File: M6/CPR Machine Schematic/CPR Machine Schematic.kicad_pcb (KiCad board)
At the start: 2 copper layers, 79.8 x 63 mm, 78 parts, among them J1 Battery 22.2V IN, J10 Stop Button Port, J11 Go Button Port, J12 I2C Port, J13 Raspberry_Pi_2_3, J15 Conn_02x20_Odd_Even, J2 5V Spare Headers, J3 Power Switch, J4 3V3 Spare Headers, J5 12 Spare headers, J6 Battery Spare headers, J7 GND Spare Headers, J8 Force Sensor, J9 Laser Port, Q2 SSM3J332R, Q3 T2N7002BK,LM, Q4 DMMT5401 PNP, Q5 DMMT5401 PNP, Q6 T2N7002BK,LM, Q7 T2N7002BK,LM, Q8 DMG2305UX-EV, U2 MAX42403AFLB+, U3 MCP6004, U4 12V Buck, U5 MCP3021A0T-E_OT, U6 3.3V Buck

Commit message: XT30 Connectors to battery instead of screw term
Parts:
- J1, J3: footprint TerminalBlock:TerminalBlock_MaiXu_MX126-5.0-02P_1x02_P5.00mm -> Connector_AMASS:AMASS_XT30PW-M_1x02_P2.50mm_Horizontal
- moved TP4 9.79 mm to (125.0, 75.5)
- moved TP1 6.11 mm to (130.8, 75.5)
- moved TP3 5.92 mm to (118.1, 82.5)
- moved U6 5.75 mm to (126.8, 88.0)
- moved TP2 5.58 mm to (118.1, 88.9)
- moved J3 4.62 mm to (118.5, 97.0), turned to 90 degrees
- moved J1 1.86 mm to (118.5, 111.5), turned to 90 degrees
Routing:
- net +12V: track 83.3 -> 86.3 mm, vias 2 -> 3
- net +3.3V: track 189.4 -> 186.4 mm
- net /Power/From Switch: track 12.5 -> 15.5 mm
- net +22.2V: track 133.1 -> 130.6 mm
- net /Power/Battery +: track 7.47 -> 9.03 mm
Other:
- board size 79.8 x 63 mm -> 89.9 x 63 mm

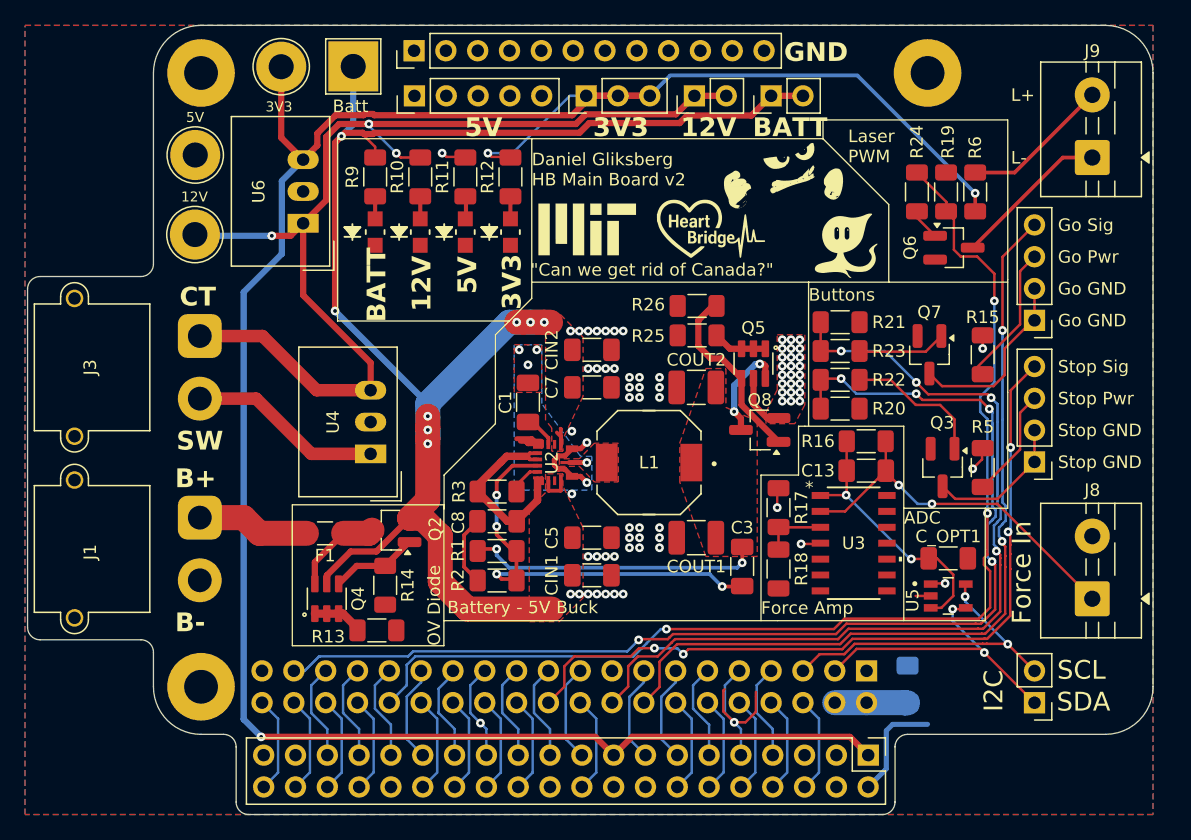
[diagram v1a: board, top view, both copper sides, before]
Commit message: Updated ADC Logic Level, Redone Layout, Geographic Reannotation
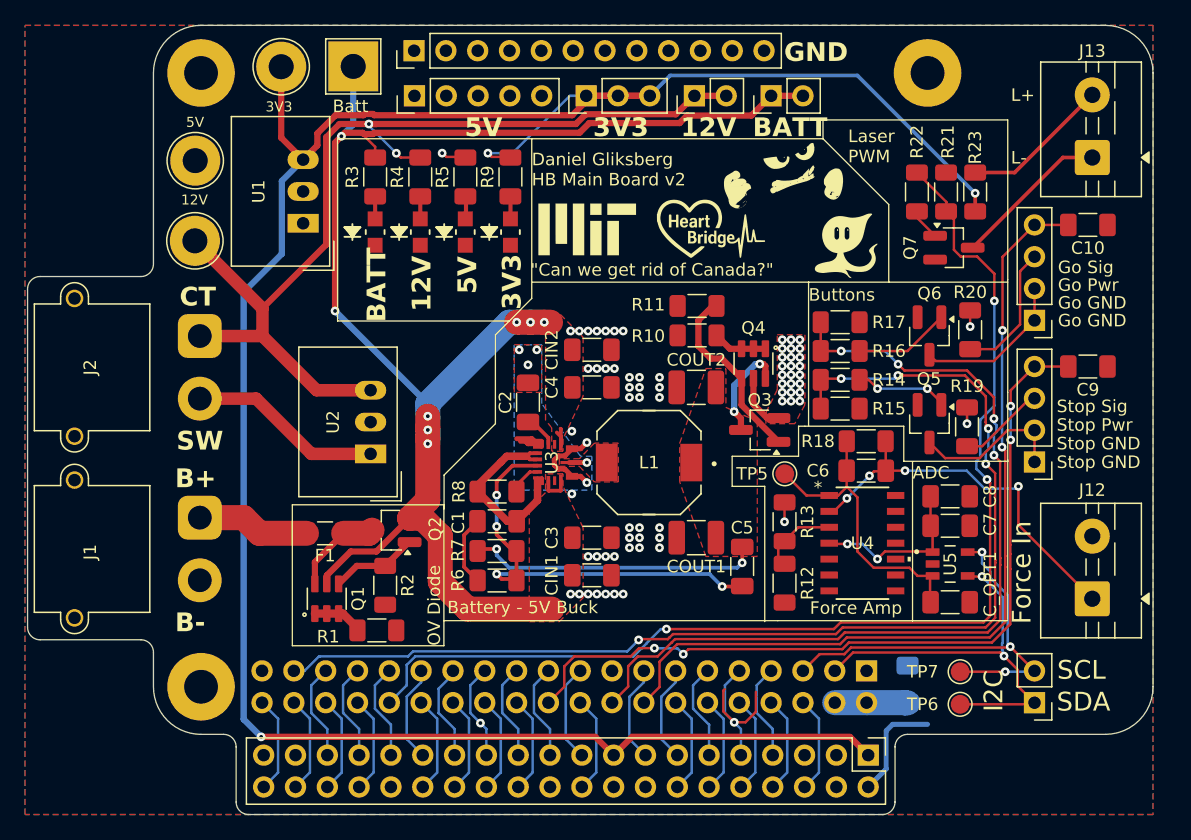
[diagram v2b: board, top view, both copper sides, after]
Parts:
- added C10: 100 nF, Capacitor_SMD:C_1206_3216Metric_Pad1.33x1.80mm_HandSolder, F.Cu at (189.4, 88.1)
- added C7: 0.1 uF, Capacitor_SMD:C_1206_3216Metric_Pad1.33x1.80mm_HandSolder, F.Cu at (178.4, 112.2)
- added C8: 10 uF, Capacitor_SMD:C_1206_3216Metric_Pad1.33x1.80mm_HandSolder, F.Cu at (178.4, 109.8)
- added C9: 100 nF, Capacitor_SMD:C_1206_3216Metric_Pad1.33x1.80mm_HandSolder, F.Cu at (189.4, 99.4)
- added TP5: Amp Out, TestPoint:TestPoint_Pad_D1.5mm, F.Cu at (165.2, 108.0)
- added TP6: SDA, TestPoint:TestPoint_Pad_D1.5mm, F.Cu at (179.2, 126.4)
- added TP7: SCL, TestPoint:TestPoint_Pad_D1.5mm, F.Cu at (179.2, 123.8)
- moved Q5 3.65 mm to (176.8, 104.0)
- moved C_OPT1 3.50 mm to (178.4, 118.2)
- moved R19 3.48 mm to (179.8, 104.2)
- moved U5 2.55 mm to (178.4, 115.2)
- moved R20 2.24 mm to (180.0, 96.5)
- moved Q6 1.50 mm to (176.8, 97.0)
- moved R12 1.23 mm to (165.2, 116.7)
- moved R13 1.23 mm to (165.2, 111.8)
- moved U4 0.70 mm to (171.4, 113.5)
- moved TP1 0.50 mm to (118.1, 89.4)
- moved TP2 0.45 mm to (118.1, 83.0)
- renumbered C8 to C1, C1 to C2, C5 to C3, C7 to C4, C3 to C5, C13 to C6, H4 to H1, H3 to H2, H1 to H3, J8 to J12, J9 to J13, J13 to J14, J3 to J2, J2 to J3, J7 to J4, J4 to J5, J5 to J6, J6 to J7, J15 to J8, J12 to J9, Q4 to Q1, Q8 to Q3, Q5 to Q4, Q3 to Q5, Q7 to Q6, Q6 to Q7, R13 to R1, R25 to R10, R26 to R11, R18 to R12, R17 to R13, R22 to R14, R20 to R15, R23 to R16, R21 to R17, R16 to R18, R5 to R19, R14 to R2, R15 to R20, R19 to R21, R24 to R22, R6 to R23, R9 to R3, R10 to R4, R11 to R5, R2 to R6, R1 to R7, R3 to R8, R12 to R9, TP2 to TP1, TP3 to TP2, TP4 to TP3, TP1 to TP4, U6 to U1, U4 to U2, U2 to U3, U3 to U4
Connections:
- U1 pad 1: +12V -> +5V
- U4 pad 4: +5V -> +3V3
- U5 pad 1: +5V -> +3V3
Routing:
- net +3V3: track 0.00 -> 13.6 mm, vias 0 -> 2
- net /Raspi/I2C_SCL: track 26.5 -> 35.7 mm, vias 2 -> 3
- net /Raspi/I2C_SDA: track 24.1 -> 33.2 mm
- net +12V: track 86.3 -> 80.2 mm, vias 3 -> 2
- net +5V: track 22.7 -> 19.3 mm, vias 30 -> 28
- net Net-(Q3-G): track 11.2 -> 8.18 mm, vias 0 -> 2
- net /HMI_Raspi/Stop Button: track 62.0 -> 64.9 mm
- net Net-(U5-AIN): track 21.5 -> 24.3 mm, vias 2 -> 0
- net /HMI_Raspi/Go Button: track 65.6 -> 68.3 mm
- net /HMI_Raspi/Go Button Ground: track 14.8 -> 12.5 mm
- net /HMI_Raspi/Stop LED Power: track 8.79 -> 6.97 mm
- net GND: track 79.4 -> 78.2 mm
- net Net-(J8-Pin_1): track 29.7 -> 30.9 mm, vias 2 -> 4
- net /Sensing/Vref: track 5.15 -> 6.27 mm
- net /HMI_Raspi/Stop Button Ground: track 11.5 -> 12.4 mm
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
